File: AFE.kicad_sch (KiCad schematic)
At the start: 37 parts, among them J2 Conn_01x08, J3 Conn_01x01, J4 Conn_01x01, U10 ADS1015IDGSR, U11 ADS1015IDGSR, U6 AP358SG-13, U7 SM05T1G

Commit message: Finalized schematic
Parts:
- removed C43, C44: 0.1u, symbol Device:C
- removed J2: Conn_01x08, symbol Connector_Generic:Conn_01x08
- removed J3, J4: Conn_01x01, symbol Connector_Generic:Conn_01x01
- removed R18, R19, R20, R21: 2k, symbol Device:R
- removed U10, U11: ADS1015IDGSR, DGS0010A_N, symbol TeenieWeenie:ADS1015IDGSR
- added J2, J7: Conn_01x02, symbol Connector_Generic:Conn_01x02
- added TP1 (x2): TestPoint, TestPoint:TestPoint_Pad_1.5x1.5mm, symbol Connector:TestPoint
- added U10: SM05T1G, TeenieWeenieLibrary:SOT-23_ONS, symbol TeenieWeenie:SM05T1G
- added U11: AP358SG-13, TeenieWeenieLibrary:SOP-8L_DIO, symbol TeenieWeenie:AP358SG-13
- C24, C25, C26, C27, C28, C29, C30, C31: footprint (none) -> Capacitor_SMD:C_0402_1005Metric
- C35, C36: value 160p -> 4.7u; footprint (none) -> Capacitor_SMD:C_0402_1005Metric; now not fitted; now left out of the parts list
- C37, C39: value 160p -> 16p; footprint (none) -> Capacitor_SMD:C_0402_1005Metric; now not fitted; now left out of the parts list
- C38, C40: footprint (none) -> Capacitor_SMD:C_0402_1005Metric; now not fitted; now left out of the parts list
- C41: value 160p -> 10u; footprint (none) -> Capacitor_SMD:C_0402_1005Metric; now not fitted; now left out of the parts list
- C42: value 160p -> 0.1u; footprint (none) -> Capacitor_SMD:C_0402_1005Metric; now not fitted; now left out of the parts list
- R10, R11, R12, R9: footprint (none) -> Resistor_SMD:R_0402_1005Metric
- R13, R16: value 2k -> 7.42k; footprint (none) -> Resistor_SMD:R_0402_1005Metric; now not fitted; now left out of the parts list
- R15, R17: value 2k -> 133k; footprint (none) -> Resistor_SMD:R_0402_1005Metric; now not fitted; now left out of the parts list
- U6: footprint SOP-8L_DIO -> TeenieWeenieLibrary:SOP-8L_DIO
- U7: footprint SOT-23_ONS -> TeenieWeenieLibrary:SOT-23_ONS
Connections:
- net AIN1_1 is gone; now on net +3V3: C42.1
- net AIN2_1 is gone; now on an unnamed net: C40.1
- net AIN3_1 is gone; now on net +3V3: C41.1
- net POT2 is gone; now on an unnamed net: R15.1
- net POT4 is gone; now on an unnamed net: R17.1
- net +3V3: now also U11.8 (V+)
- net NONINV_IN1_0: now reaches R10.2
- net NONINV_IN1_0: now also U6.3 (NON-INVERTINGINPUT1)
- net NONINV_IN2_0: now reaches R12.2, U6.5 (NON-INVERTINGINPUT2)
- net AFE_L renamed AFE0_L
- net AFE_R renamed AFE0_R
- net AIN0_0: no longer names the net of R13.2
- net AIN0_0: now also C37.1, C38.1; no longer C35.1
- net AIN0_1: no longer names the net of C39.1
- net AIN0_1: now also R16.2
- net AIN1_0 renamed NONINV_IN1_1
- net NONINV_IN1_1: now also U11.3 (NON-INVERTINGINPUT1); no longer C38.1
- net AIN2_0: no longer names the net of C36.1
- net AIN2_0: now also J7.1 (Pin_1), U10.1 (CATHODE); no longer R16.2
- net AIN3_0 renamed NONINV_IN2_1
- net NONINV_IN2_1: now also U11.5 (NON-INVERTINGINPUT2); no longer C37.1
- net AudioIn_L: no longer names the net of U7.1 (CATHODE)
- net AudioIn_L: now also C30.1, J2.1 (Pin_1), TP1.1; no longer C29.1
- net AudioIn_R: no longer names the net of U7.2 (CATHODE)
- net AudioIn_R: now also C29.1, J2.2 (Pin_2), TP1.1; no longer C30.1
- net GNDA renamed GND
- net GND: now also U10.3 (ANODE), U11.4 (GND); no longer C35.2, C36.2, C38.2, C40.2
- net POT1: no longer names the net of R13.1
- net POT1: now also C35.2
- net POT3: no longer names the net of R16.1
- net POT3: now also C36.2
- new net: C35.1, J7.2 (Pin_2), U10.2 (CATHODE)
- new net AFE1_L: C38.2, U11.1 (OUTPUT1), U11.2 (INVERTINGINPUT1)
- new net AFE1_R: C40.2, U11.6 (INVERTINGINPUT2), U11.7 (OUTPUT2)
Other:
- note added: "2-Pole LPF fs=1MHz"
- note added: "Audio In"
- moved on the sheet: C24, C25, C26, C27, C28, C29, C30, C31, R10, R11, R12, R9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

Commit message: Added pots to schem
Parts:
- J2: now left out of the parts list
- J7: now not fitted; now left out of the parts list
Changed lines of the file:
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@@
   )
   (symbol (lib_id "Connector_Generic:Conn_01x02") (at 17.78 52.07 180) (unit 1)
-    (in_bom yes) (on_board yes) (dnp no) (fields_autoplaced)
+    (in_bom no) (on_board yes) (dnp no) (fields_autoplaced)
     (property "Reference" "J2" (at 17.78 43.18 0)
       (effects (font (size 1.27 1.27)))
@@
   )
   (symbol (lib_id "Connector_Generic:Conn_01x02") (at 17.78 120.65 180) (unit 1)
-    (in_bom yes) (on_board yes) (dnp no) (fields_autoplaced)
+    (in_bom no) (on_board yes) (dnp yes) (fields_autoplaced)
     (property "Reference" "J7" (at 17.78 111.76 0)
       (effects (font (size 1.27 1.27)))

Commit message: final final schematic:
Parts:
- removed J2: Conn_01x02, symbol Connector_Generic:Conn_01x02
- J7: footprint (none) -> Connector_PinHeader_1.00mm:PinHeader_1x02_P1.00mm_Horizontal
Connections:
- net AudioIn_R: now reaches C30.1, TP1.1, U7.1 (CATHODE)
- net AudioIn_L: now reaches C29.1, TP1.1, U7.2 (CATHODE)
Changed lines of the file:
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@@
     (effects (font (size 1.27 1.27)) (justify left bottom))
+  )
+  (hierarchical_label "AudioIn_R" (shape input) (at 22.86 52.07 180) (fields_autoplaced)
+    (effects (font (size 1.27 1.27)) (justify right))
   )
   (hierarchical_label "AFE0_R" (shape output) (at 256.54 53.34 0) (fields_autoplaced)
@@
     (effects (font (size 1.27 1.27)) (justify left))
   )
+  (hierarchical_label "AudioIn_L" (shape input) (at 22.86 49.53 180) (fields_autoplaced)
+    (effects (font (size 1.27 1.27)) (justify right))
+  )
   (symbol (lib_id "Device:C") (at 58.42 127 90) (unit 1)
     (in_bom no) (on_board yes) (dnp yes) (fields_autoplaced)
@@
         (path "/58e2e2d3-cf30-4313-be51-7fb67401d242/d79052ad-b30d-48cb-904a-b15d582d373d"
           (reference "C36") (unit 1)
-        )
-      )
-    )
-  )
-  (symbol (lib_id "Connector_Generic:Conn_01x02") (at 17.78 52.07 180) (unit 1)
-    (in_bom no) (on_board yes) (dnp no) (fields_autoplaced)
-    (property "Reference" "J2" (at 17.78 43.18 0)
-      (effects (font (size 1.27 1.27)))
-    )
-    (property "Value" "Conn_01x02" (at 17.78 45.72 0)
-      (effects (font (size 1.27 1.27)))
-    )
-    (property "Footprint" "" (at 17.78 52.07 0)
-      (effects (font (size 1.27 1.27)) hide)
-    )
-    (property "Datasheet" "~" (at 17.78 52.07 0)
-      (effects (font (size 1.27 1.27)) hide)
-    )
-    (pin "1")
-    (pin "2")
-    (instances
-      (project "TeenieWeenie"
-        (path "/58e2e2d3-cf30-4313-be51-7fb67401d242/d79052ad-b30d-48cb-904a-b15d582d373d"
-          (reference "J2") (unit 1)
         )
       )
@@
       (effects (font (size 1.27 1.27)))
     )
-    (property "Footprint" "" (at 17.78 120.65 0)
-      (effects (font (size 1.27 1.27)) hide)
-    )
+    (property "Footprint" "Connector_PinHeader_1.00mm:PinHeader_1x02_P1.00mm_Horizontal" (at 17.78 120.65 0)
+      (effects (font (size 1.27 1.27)) hide)
+    )

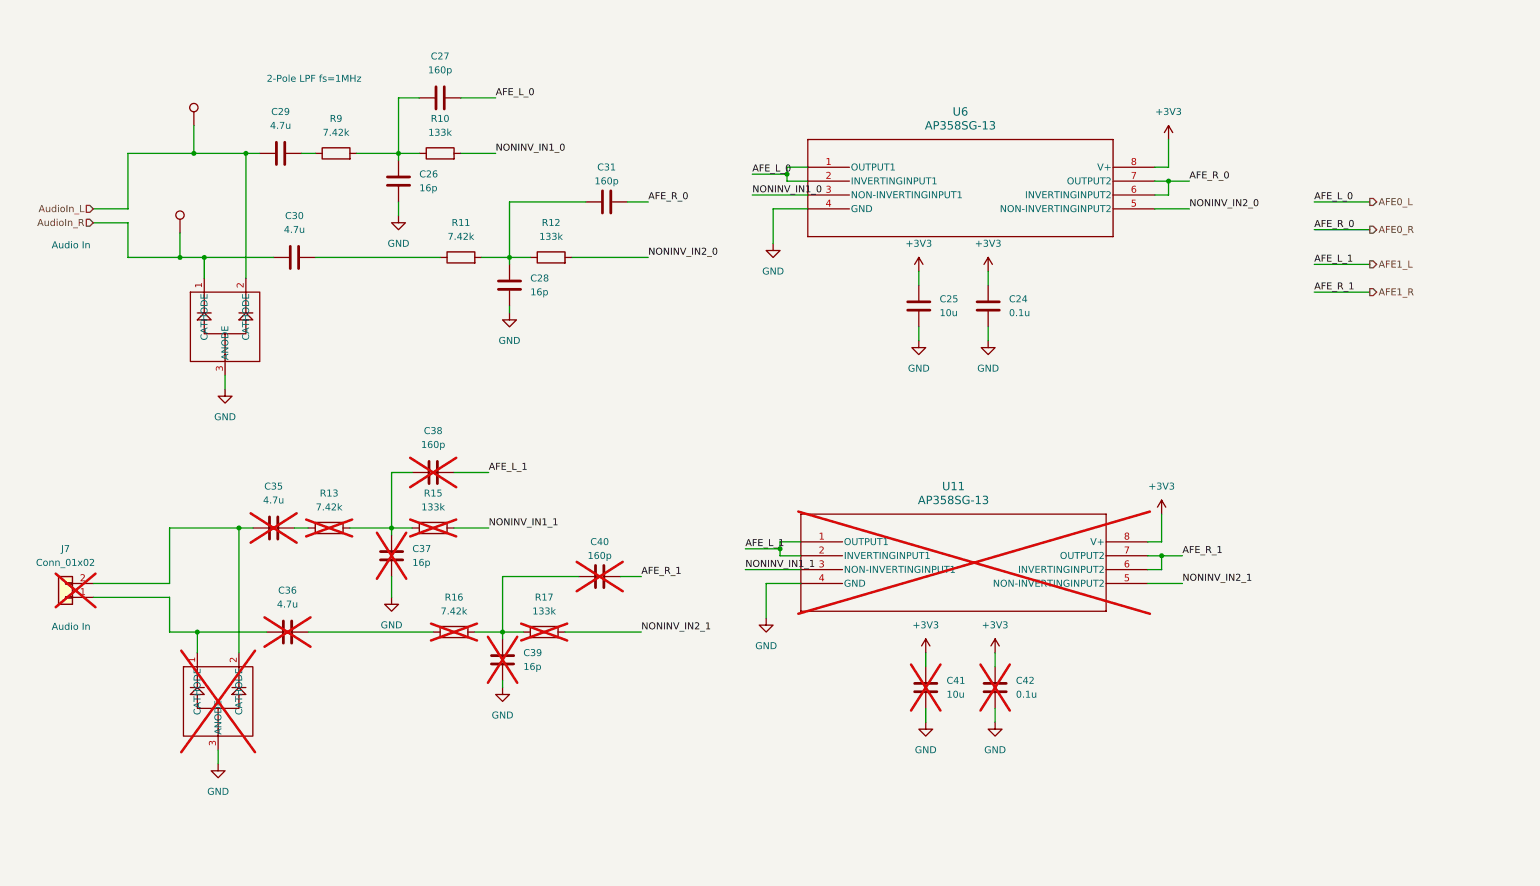
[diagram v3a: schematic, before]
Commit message: rev1 of pcb component placement
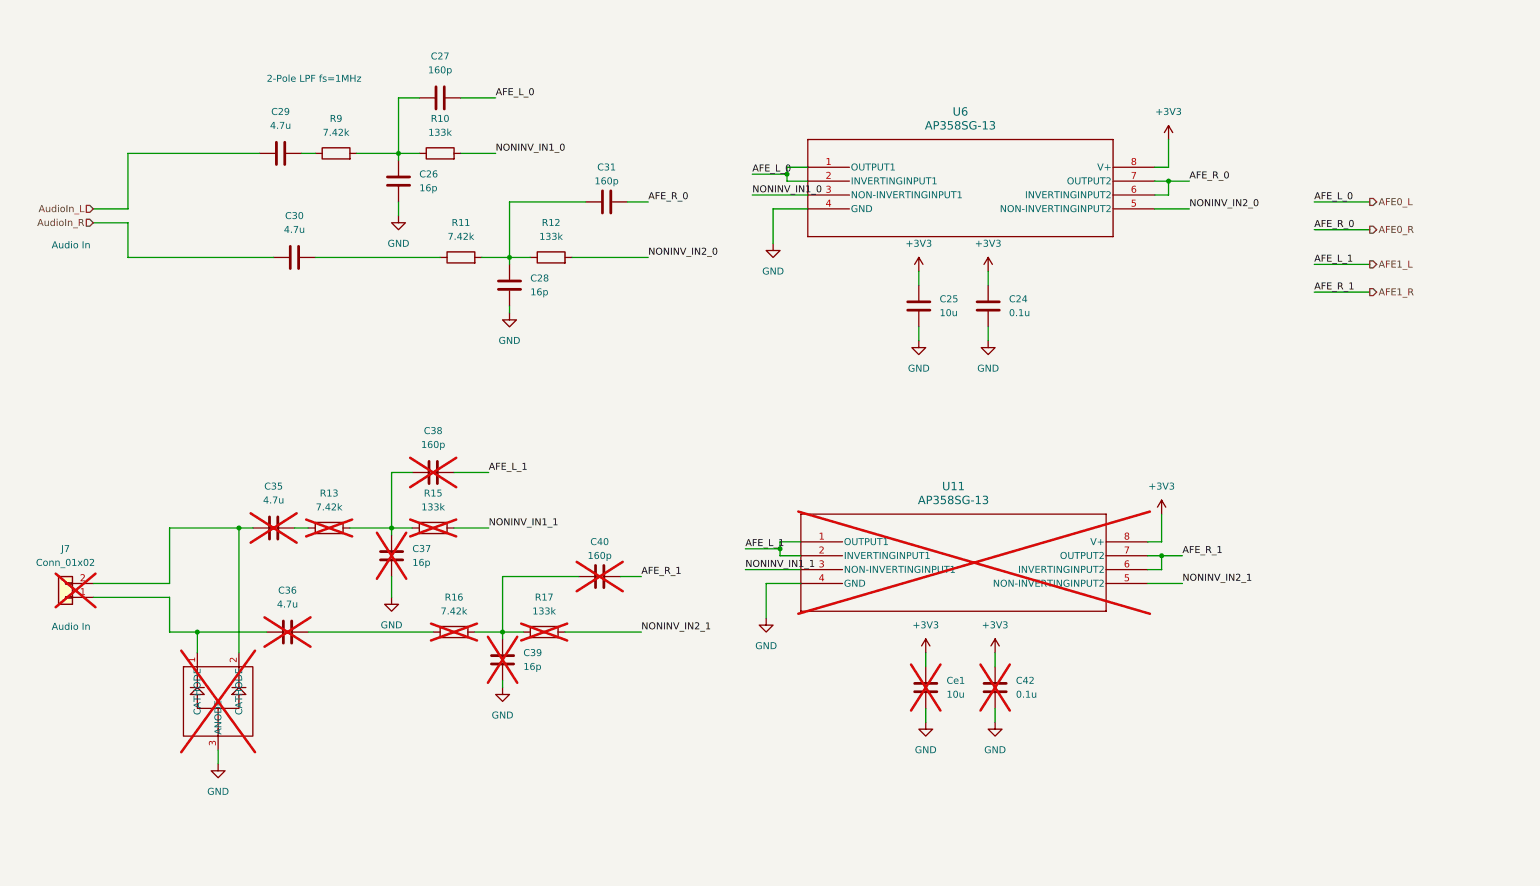
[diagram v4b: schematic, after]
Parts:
- removed TP1 (x2): TestPoint, TestPoint:TestPoint_Pad_1.5x1.5mm, symbol Connector:TestPoint
- removed U7: SM05T1G, TeenieWeenieLibrary:SOT-23_ONS, symbol TeenieWeenie:SM05T1G
- renumbered C41 to Ce1

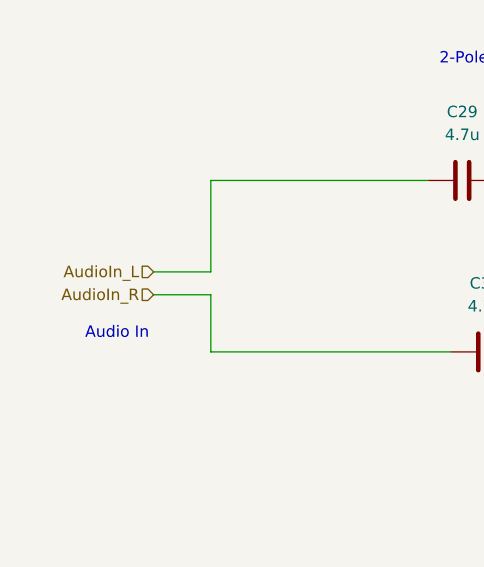
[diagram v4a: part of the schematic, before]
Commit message: routed power
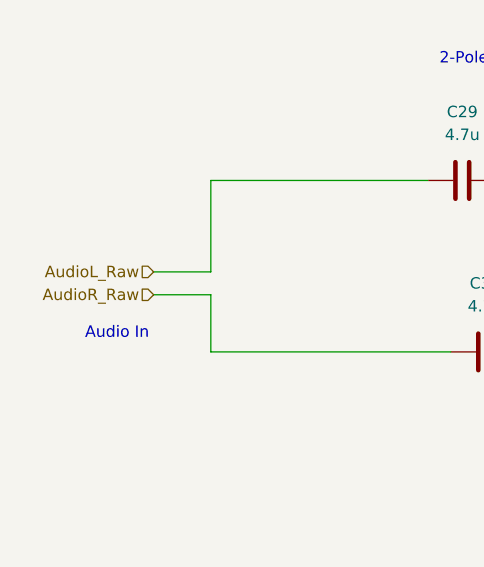
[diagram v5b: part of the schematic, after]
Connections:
- net AudioIn_L renamed AudioL_Raw
- net AudioIn_R renamed AudioR_Raw
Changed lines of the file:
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@@
     (effects (font (size 1.27 1.27)) (justify left bottom))
   )
-  (hierarchical_label "AudioIn_R" (shape input) (at 22.86 52.07 180) (fields_autoplaced)
+  (hierarchical_label "AudioR_Raw" (shape input) (at 22.86 52.07 180) (fields_autoplaced)
     (effects (font (size 1.27 1.27)) (justify right))
   )
@@
     (effects (font (size 1.27 1.27)) (justify left))
   )
-  (hierarchical_label "AudioIn_L" (shape input) (at 22.86 49.53 180) (fields_autoplaced)
+  (hierarchical_label "AudioL_Raw" (shape input) (at 22.86 49.53 180) (fields_autoplaced)
     (effects (font (size 1.27 1.27)) (justify right))
   )

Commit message: redesign layout
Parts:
- added C13, C22, C5: 1u, Capacitor_SMD:C_0402_1005Metric, symbol Device:C
- added C14: 100n, Capacitor_SMD:C_0402_1005Metric, symbol Device:C
- added R41, R42, R43, R44, R45, R46: 10k, Resistor_SMD:R_0402_1005Metric, symbol Device:R
- added R47, R48: 1M, Resistor_SMD:R_0402_1005Metric, symbol Device:R
- C26, C28: value 16p -> 10p
- C27, C31: value 160p -> 100p
- R10, R12: value 133k -> 31.1k
- R11, R9: value 7.42k -> 1k
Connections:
- net +3V3: now also R43.2
- net AFE0_L: now also C31.2, R41.2; no longer C27.2, U6.2 (INVERTINGINPUT1)
- net AFE0_R: now also C27.2, R46.2; no longer C31.2, U6.6 (INVERTINGINPUT2)
- net GND: now also C13.2, C14.2, R44.1; no longer C26.2, C28.2
- net at C31.1, R11.2, R12.1: no longer C28.1
- net at C27.1, R10.1, R9.2: no longer C26.1
- net at C30.2, R11.1: now also R47.2
- net at C29.2, R9.1: now also R48.2
- net NONINV_IN1_0 renamed IN1-A
- net IN1-A: now also R41.1, R42.2; no longer R10.2
- net NONINV_IN2_0 renamed IN1+A
- net IN1+A: now also C28.1, U6.2 (INVERTINGINPUT1); no longer U6.5 (NON-INVERTINGINPUT2)
- new net: C22.2, R45.1
- new net: C5.2, R42.1
- new net IN2+A: C26.1, R10.2, U6.5 (NON-INVERTINGINPUT2)
- new net IN2-A: R45.2, R46.1, U6.6 (INVERTINGINPUT2)
- new net Vdd2: C13.1, C14.1, C22.1, C26.2, C28.2, C5.1, R43.1, R44.2, R47.1, R48.1
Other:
- moved on the sheet: C24, C25, C28, C30, C31, C35, C36, C37, C38, C39, C40, C42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
